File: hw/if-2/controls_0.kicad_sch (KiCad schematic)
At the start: 9 parts, among them U12 LTV-356T, U6 LTV-356T, U8 LTV-356T

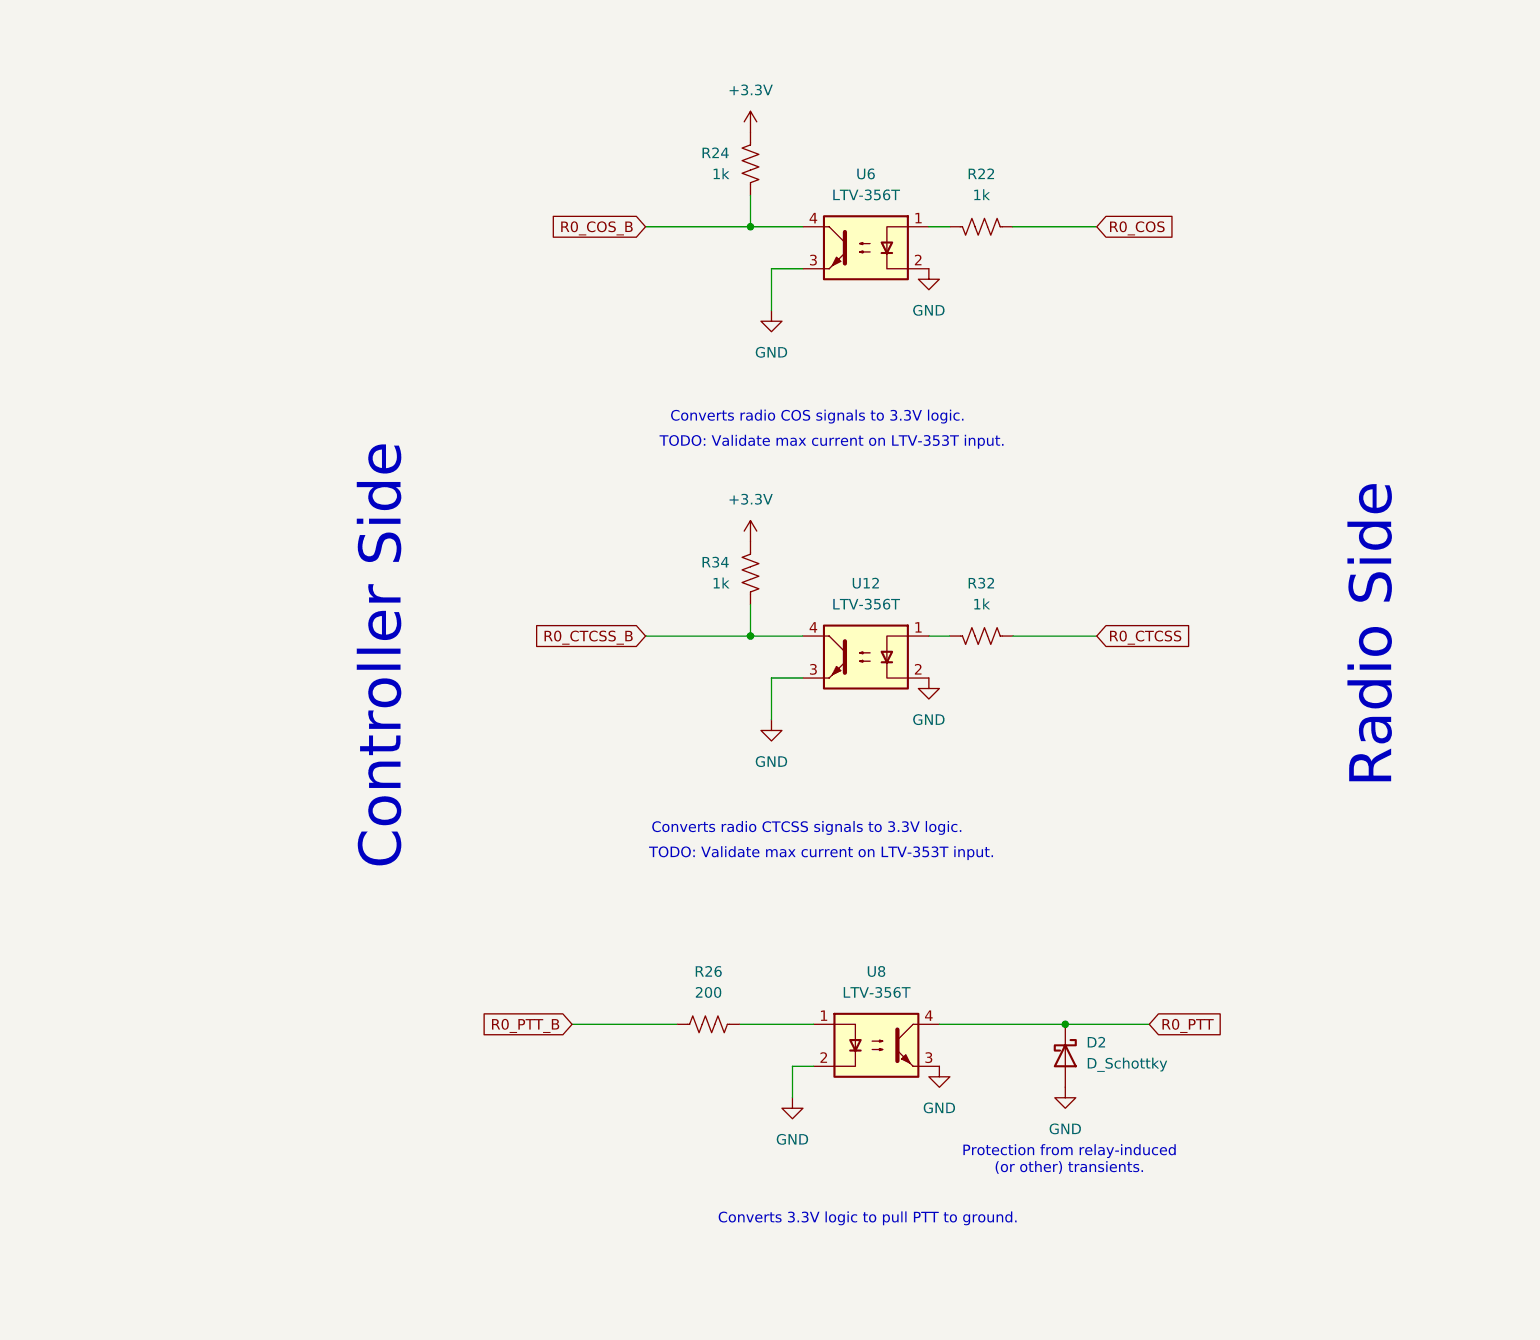
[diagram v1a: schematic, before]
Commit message: Ready to do layout on IF2 board
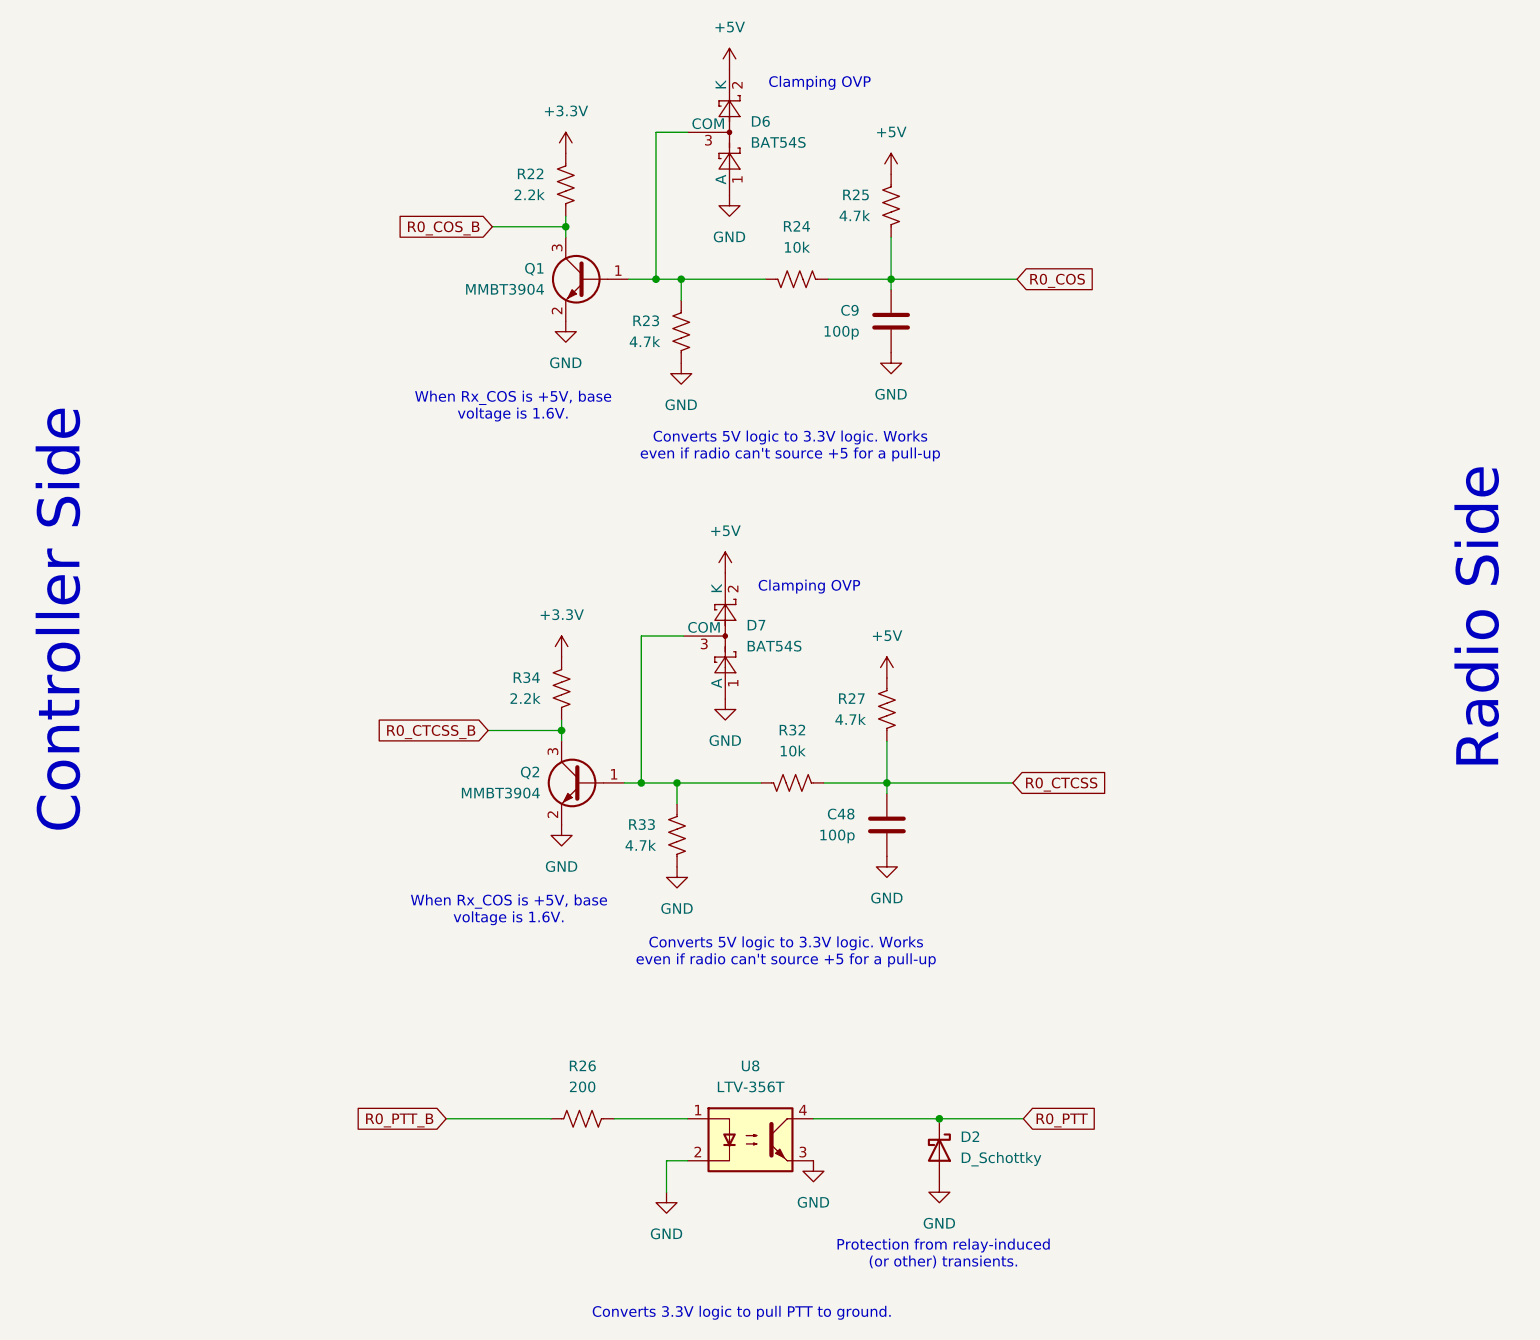
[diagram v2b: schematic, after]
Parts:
- removed U12, U6: LTV-356T, Package_SO:SO-4_4.4x3.6mm_P2.54mm, symbol Isolator:LTV-356T
- added C48, C9: 100p, symbol Device:C
- added D6, D7: BAT54S, Package_TO_SOT_SMD:SOT-23, symbol Diode:BAT54S
- added Q1, Q2: MMBT3904, Package_TO_SOT_SMD:SOT-23, symbol Transistor_BJT:MMBT3904
- added R23, R25, R27, R33: 4.7k, symbol Device:R_US
- R22, R34: value 1k -> 2.2k; footprint Resistor_SMD:R_0805_2012Metric_Pad1.20x1.40mm_HandSolder -> (none)
- R24, R32: value 1k -> 10k; footprint Resistor_SMD:R_0805_2012Metric_Pad1.20x1.40mm_HandSolder -> (none)
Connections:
- net +3.3V: now also R22.1; no longer R24.1
- net GND: now also C48.2, C9.2, D6.1 (A), D7.1 (A), Q1.2 (E), Q2.2 (E), R23.2, R33.2
- net R0_COS: now also R24.1, C9.1, R25.2; no longer R22.1
- net R0_COS_B: now also R22.2, Q1.3 (C); no longer R24.2
- net R0_CTCSS: now also C48.1, R27.2
- net R0_CTCSS_B: now also Q2.3 (C)
- net at R32.2: now also D7.3 (COM), Q2.1 (B), R33.1
- new net: D6.3 (COM), Q1.1 (B), R23.1, R24.2
- new net +5V: D6.2 (K), D7.2 (K), R25.1, R27.1
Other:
- note added: "Clamping OVP"
- note added: "Converts 5V logic to 3.3V logic. Works even if radio can't source +5 for a pull-up"
- note added: "When Rx_COS is +5V, base voltage is 1.6V."
- note removed: "Converts radio COS signals to 3.3V logic."
- note removed: "Converts radio CTCSS signals to 3.3V logic."
- note removed: "TODO: Validate max current on LTV-353T input."
- moved on the sheet: D2, R26, U8

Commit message: Ready to do layout on IF2 board
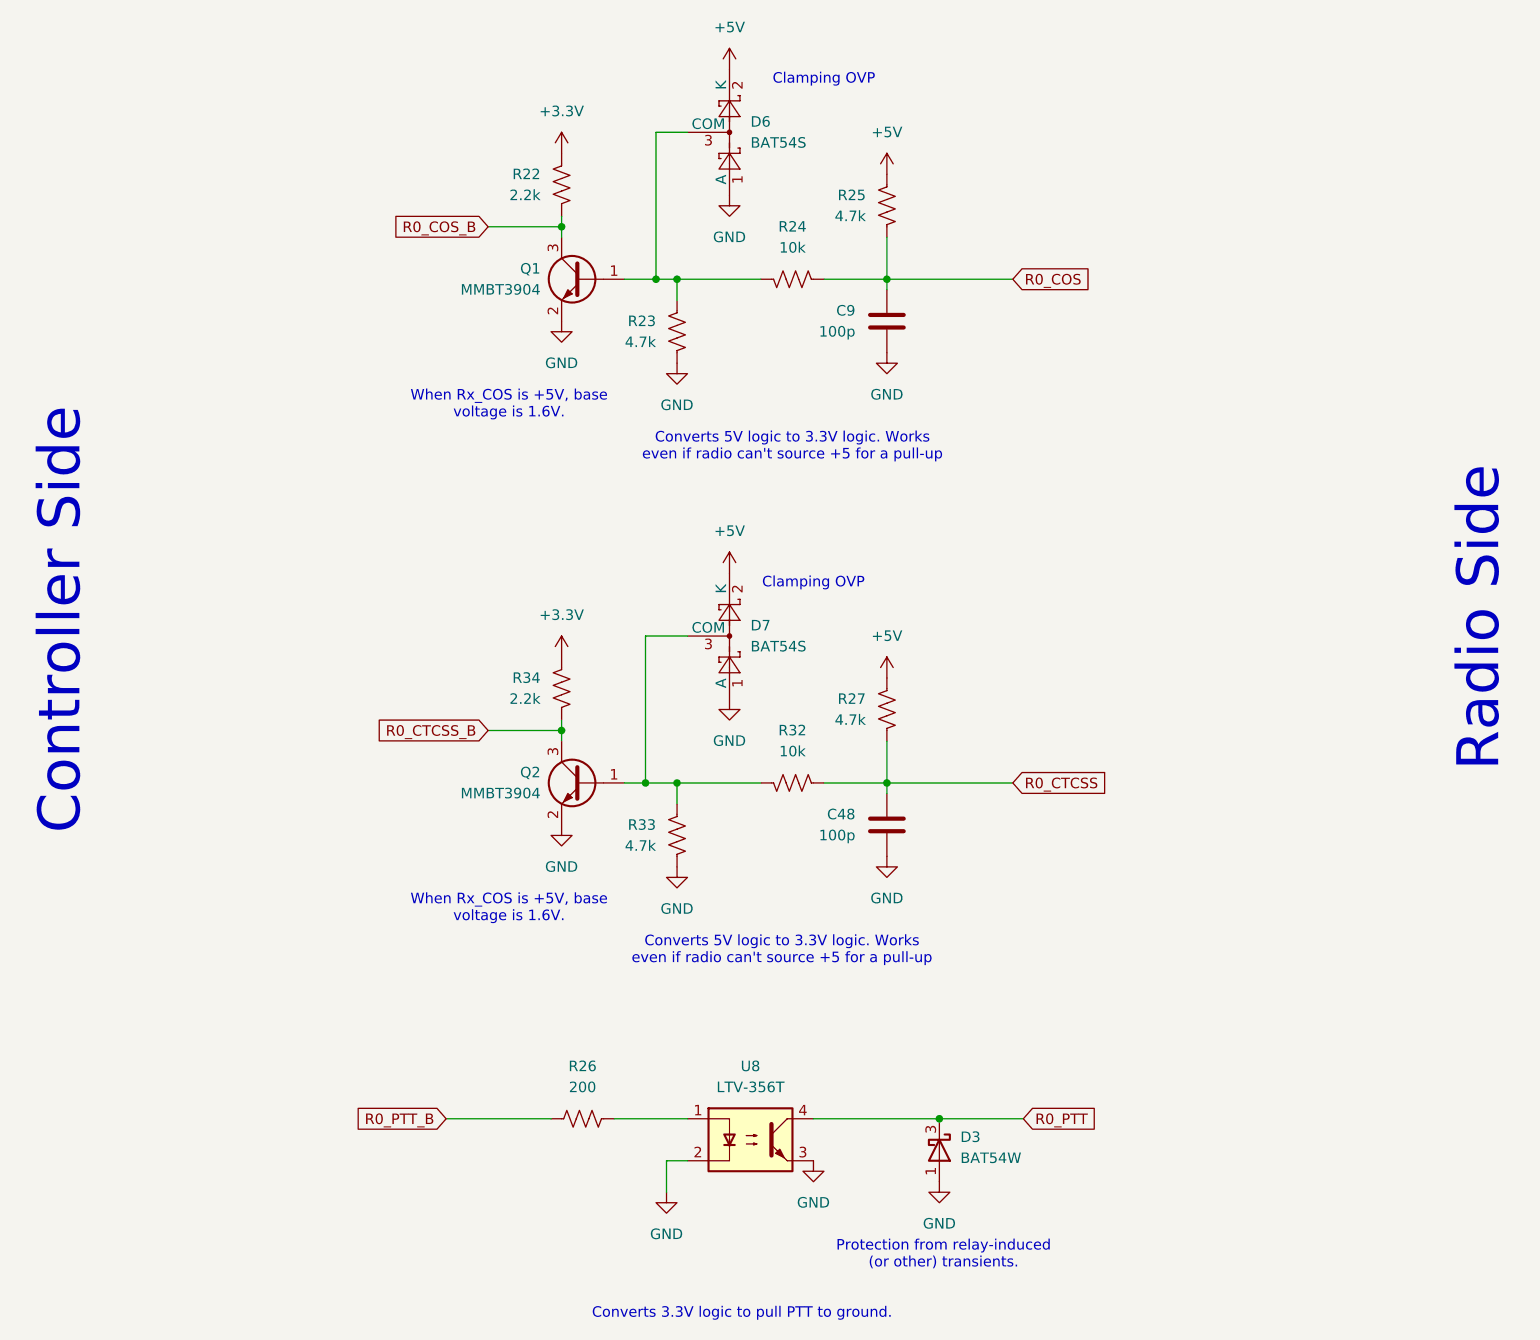
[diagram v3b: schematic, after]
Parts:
- removed D2: D_Schottky, symbol Device:D_Schottky
- added D3: BAT54W, Package_TO_SOT_SMD:SOT-323_SC-70, symbol Diode:BAT54W
- C48, C9: footprint (none) -> Capacitor_SMD:C_0805_2012Metric_Pad1.18x1.45mm_HandSolder
- R22, R23, R24, R25, R27, R32, R33, R34: footprint (none) -> Resistor_SMD:R_0805_2012Metric_Pad1.20x1.40mm_HandSolder
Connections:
- net GND: now also D3.1 (A)
- net R0_PTT: now also D3.3 (K)
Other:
- title: COS/CTCSS/PTT Controls (Radio 0) -> COS/CTCSS/PTT Controls (Radio 1)
- moved on the sheet: C9, D7, Q1, R22, R23, R24, R25

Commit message: Making progress on layout
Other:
- title: COS/CTCSS/PTT Controls (Radio 1) -> COS/CTCSS/PTT Controls (Radio 0)
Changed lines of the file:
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@@
 	(paper "USLetter")
 	(title_block
-		(title "COS/CTCSS/PTT Controls (Radio 1)")
-		(date "2025-03-18")
+		(title "COS/CTCSS/PTT Controls (Radio 0)")
+		(date "2025-05-09")
 		(rev "2")
 		(company "Bruce MacKinnon KC1FSZ")

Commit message: Making progress on layout
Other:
- moved on the sheet: C48, C9, D3, D6, D7, Q1, Q2, R22, R23, R24, R25, R26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
